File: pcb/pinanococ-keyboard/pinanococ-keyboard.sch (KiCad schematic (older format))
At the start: 70 parts, among them J1 AudioJack4, SW1 SW_Push, SW10 SW_Push, SW11 SW_Push, SW12 SW_Push, SW14 SW_Push, SW15 SW_Push, SW16 SW_Push, SW17 SW_Push, SW18 SW_Push, SW2 SW_Push, SW20 SW_Push_Dual_x2, SW21 SW_Push, SW22 SW_Push, SW23 SW_Push, SW24 SW_Push, SW26 SW_Push_Dual_x2, SW27 SW_Push, SW28 SW_Push, SW29 SW_Push, SW3 SW_Push, SW30 SW_Push, SW32 SW_Push_Dual_x2, SW33 SW_Push, SW34 SW_Push, SW35 SW_Push, SW36 SW_Push, SW37 SW_Push, SW38 Rotary_Encoder_Switch, SW4 SW_Push, SW5 SW_Push, SW6 SW_Push, SW8 SW_Push, SW9 SW_Push, U1 Pico

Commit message: pcb component layout
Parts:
- removed SW14: SW_Push, keyswitches:SW_PG1350, symbol Switch:SW_Push
- added D13: D_ALT, Diode_THT:D_DO-34_SOD68_P7.62mm_Horizontal, symbol Device:D_ALT
- added SW14: SW_Push_Dual_x2, keyswitches:SW_PG1350_double_rotate, symbol Switch:SW_Push_Dual_x2
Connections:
- net COL_2: now also D13.1 (K)
- net ROW_0: now also SW14.4 (D)
- net ROW_1: now also SW14.2 (D)
- net at D14.2 (A): now also SW14.1 (C)
- new net: D13.2 (A), SW14.3 (C)
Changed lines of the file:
@@
-	0    1    1    0
-$EndComp
-$Comp
-L Switch:SW_Push SW14
-U 1 1 61CB00FC
-P 2800 3150
-F 0 "SW14" V 2754 3298 50  0000 L CNN
-F 1 "SW_Push" V 2845 3298 50  0000 L CNN
-F 2 "keyswitches:SW_PG1350" H 2800 3350 50  0001 C CNN
-F 3 "~" H 2800 3350 50  0001 C CNN
-	1    2800 3150
 	0    1    1    0
 $EndComp
@@
 $EndComp
 Connection ~ 2100 3350
-Connection ~ 2800 3350
-Wire Wire Line
-	2100 3350 2800 3350
 Wire Wire Line
 	1400 3350 2100 3350
@@
 	1800 2000 1800 2950
 Wire Wire Line
-	2500 2000 2500 2950
+	2500 2000 2500 2300
 $Comp
 L Device:Rotary_Encoder_Switch SW38
@@
 	4900 3350 5400 3350
 Wire Wire Line
-	1400 2700 3500 2700
-Wire Wire Line
-	2800 3350 3500 3350
+	1400 2700 2800 2700
 $Comp
 L Switch:SW_Push_Dual_x2 SW26
@@
 Wire Wire Line
 	3500 2700 4200 2700
+Wire Wire Line
+	2100 3350 2800 3350
+$Comp
+L Device:D_ALT D13
+U 1 1 61C34EA8
+P 2650 2300
+F 0 "D13" H 2650 2517 50  0000 C CNN
+F 1 "D_ALT" H 2650 2426 50  0000 C CNN
+F 2 "Diode_THT:D_DO-34_SOD68_P7.62mm_Horizontal" H 2650 2300 50  0001 C CNN
+F 3 "~" H 2650 2300 50  0001 C CNN
+	1    2650 2300
+	1    0    0    -1
+$EndComp
+Connection ~ 2500 2300
+Wire Wire Line
+	2500 2300 2500 2950
+$Comp
+L Switch:SW_Push_Dual_x2 SW14
+U 2 1 61C35305
+P 2800 2500
+F 0 "SW14" V 2754 2648 50  0000 L CNN
+F 1 "SW_Push_Dual_x2" V 2845 2648 50  0000 L CNN
+F 2 "keyswitches:SW_PG1350_double_rotate" H 2800 2700 50  0001 C CNN
+F 3 "~" H 2800 2700 50  0001 C CNN
+	2    2800 2500
+	0    1    1    0
+$EndComp
+Connection ~ 2800 2700
+Wire Wire Line
+	2800 2700 3500 2700
+$Comp
+L Switch:SW_Push_Dual_x2 SW14
+U 1 1 61C35B95
+P 2800 3150
+F 0 "SW14" V 2754 3298 50  0000 L CNN
+F 1 "SW_Push_Dual_x2" V 2845 3298 50  0000 L CNN
+F 2 "keyswitches:SW_PG1350_double_rotate" H 2800 3350 50  0001 C CNN
+F 3 "~" H 2800 3350 50  0001 C CNN
+	1    2800 3150
+	0    1    1    0
+$EndComp
+Connection ~ 2800 3350
+Wire Wire Line
+	2800 3350 3500 3350
 $EndSCHEMATC

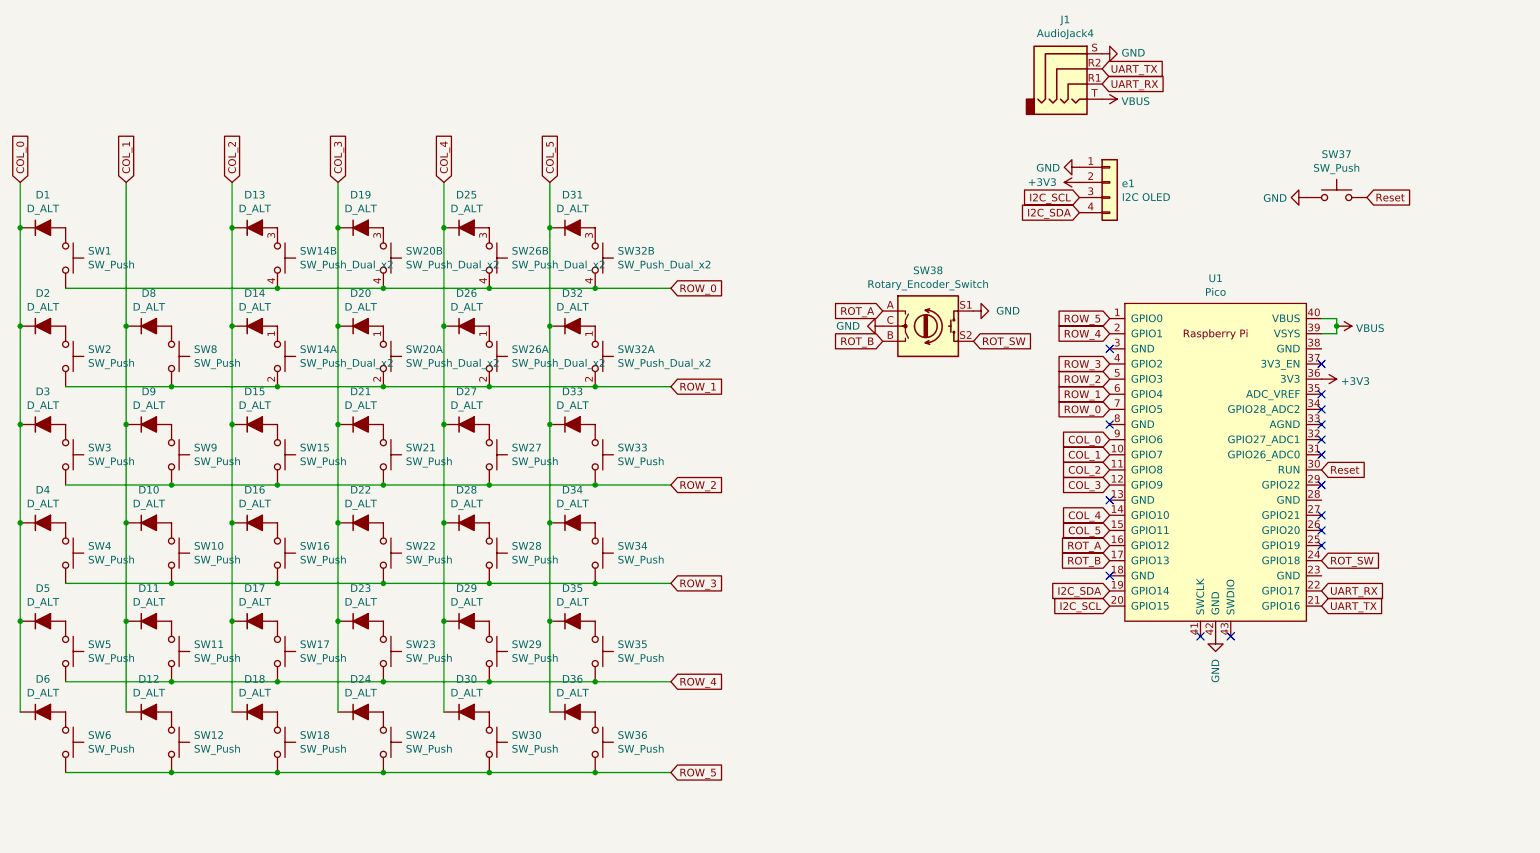
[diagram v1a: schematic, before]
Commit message: inital pcb layout with tracks
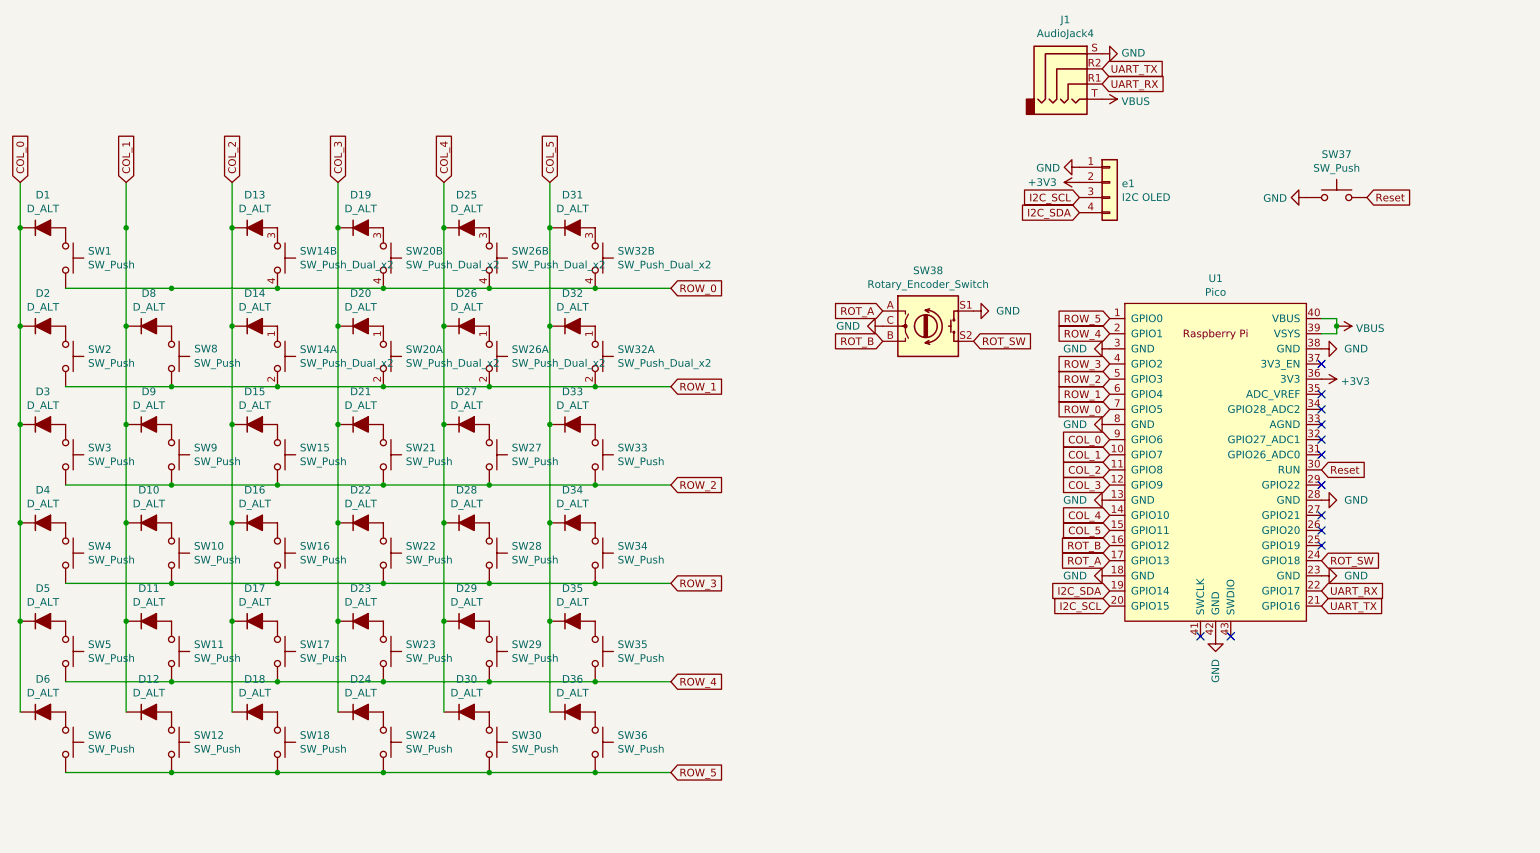
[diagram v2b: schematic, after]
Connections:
- net GND: now also U1.13 (GND), U1.18 (GND), U1.23 (GND), U1.28 (GND), U1.3 (GND), U1.38 (GND), U1.8 (GND)
- net ROT_A: now also U1.17 (GPIO13); no longer U1.16 (GPIO12)
- net ROT_B: now also U1.16 (GPIO12); no longer U1.17 (GPIO13)
- no-connect marks 16 -> 12
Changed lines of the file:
@@
 NoConn ~ 9700 3200
 NoConn ~ 9700 3400
-NoConn ~ 8300 3100
-NoConn ~ 8300 4600
-NoConn ~ 8300 4100
-NoConn ~ 8300 3600
 NoConn ~ 9700 3600
 Text GLabel 9700 4800 2    50   Input ~ 0
@@
 U 1 1 61CB00F6
 P 2100 3150
-F 0 "SW8" V 2054 3298 50  0000 L CNN
+F 0 "SW8" V 2050 3300 50  0000 L CNN
 F 1 "SW_Push" V 2145 3298 50  0000 L CNN
 F 2 "keyswitches:SW_PG1350" H 2100 3350 50  0001 C CNN
@@
 NoConn ~ 9700 3500
 Wire Wire Line
-	1800 2000 1800 2950
+	1800 2000 1800 2300
 Wire Wire Line
 	2500 2000 2500 2300
@@
 	0    1    1    0
 $EndComp
+Text GLabel 8300 4500 0    50   Input ~ 0
+ROT_A
 Text GLabel 8300 4400 0    50   Input ~ 0
-ROT_A
-Text GLabel 8300 4500 0    50   Input ~ 0
 ROT_B
 $Comp
@@
 Wire Wire Line
 	4900 3350 5400 3350
-Wire Wire Line
-	1400 2700 2800 2700
 $Comp
 L Switch:SW_Push_Dual_x2 SW26
@@
 Wire Wire Line
 	2800 3350 3500 3350
+Connection ~ 1800 2300
+Wire Wire Line
+	1800 2300 1800 2950
+Connection ~ 2100 2700
+Wire Wire Line
+	2100 2700 2800 2700
+Wire Wire Line
+	1400 2700 2100 2700
+$Comp
+L power:GND #PWR?
+U 1 1 61CBF1FB
+P 8300 3100
+F 0 "#PWR?" H 8300 2850 50  0001 C CNN
+F 1 "GND" V 8300 2950 50  0000 R CNN
+F 2 "" H 8300 3100 50  0001 C CNN
+F 3 "" H 8300 3100 50  0001 C CNN
+	1    8300 3100
+	0    1    1    0
+$EndComp
+$Comp
+L power:GND #PWR?
+U 1 1 61CC13E9
+P 8300 3600
+F 0 "#PWR?" H 8300 3350 50  0001 C CNN
+F 1 "GND" V 8300 3450 50  0000 R CNN
+F 2 "" H 8300 3600 50  0001 C CNN
+F 3 "" H 8300 3600 50  0001 C CNN
+	1    8300 3600
+	0    1    1    0
+$EndComp
+$Comp
+L power:GND #PWR?
+U 1 1 61CC1677
+P 8300 4100
+F 0 "#PWR?" H 8300 3850 50  0001 C CNN
+F 1 "GND" V 8300 3950 50  0000 R CNN
+F 2 "" H 8300 4100 50  0001 C CNN
+F 3 "" H 8300 4100 50  0001 C CNN
+	1    8300 4100
+	0    1    1    0
+$EndComp
+$Comp
+L power:GND #PWR?
+U 1 1 61CC1AD9
+P 8300 4600
+F 0 "#PWR?" H 8300 4350 50  0001 C CNN
+F 1 "GND" V 8300 4450 50  0000 R CNN
+F 2 "" H 8300 4600 50  0001 C CNN
+F 3 "" H 8300 4600 50  0001 C CNN
+	1    8300 4600
+	0    1    1    0
+$EndComp
+$Comp
+L power:GND #PWR?
+U 1 1 61CC1DF0
+P 9700 4600
+F 0 "#PWR?" H 9700 4350 50  0001 C CNN
+F 1 "GND" V 9700 4450 50  0000 R CNN
+F 2 "" H 9700 4600 50  0001 C CNN
+F 3 "" H 9700 4600 50  0001 C CNN
+	1    9700 4600
+	0    -1   -1   0
+$EndComp
+$Comp
+L power:GND #PWR?
+U 1 1 61CC27D8
+P 9700 4100
+F 0 "#PWR?" H 9700 3850 50  0001 C CNN
+F 1 "GND" V 9700 3950 50  0000 R CNN
+F 2 "" H 9700 4100 50  0001 C CNN
+F 3 "" H 9700 4100 50  0001 C CNN
+	1    9700 4100
+	0    -1   -1   0
+$EndComp
+$Comp
+L power:GND #PWR?
+U 1 1 61CC2DE6
+P 9700 3100
+F 0 "#PWR?" H 9700 2850 50  0001 C CNN
+F 1 "GND" V 9700 2950 50  0000 R CNN
+F 2 "" H 9700 3100 50  0001 C CNN
+F 3 "" H 9700 3100 50  0001 C CNN
+	1    9700 3100
+	0    -1   -1   0
+$EndComp
 $EndSCHEMATC

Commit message: reannotated flippable schematic
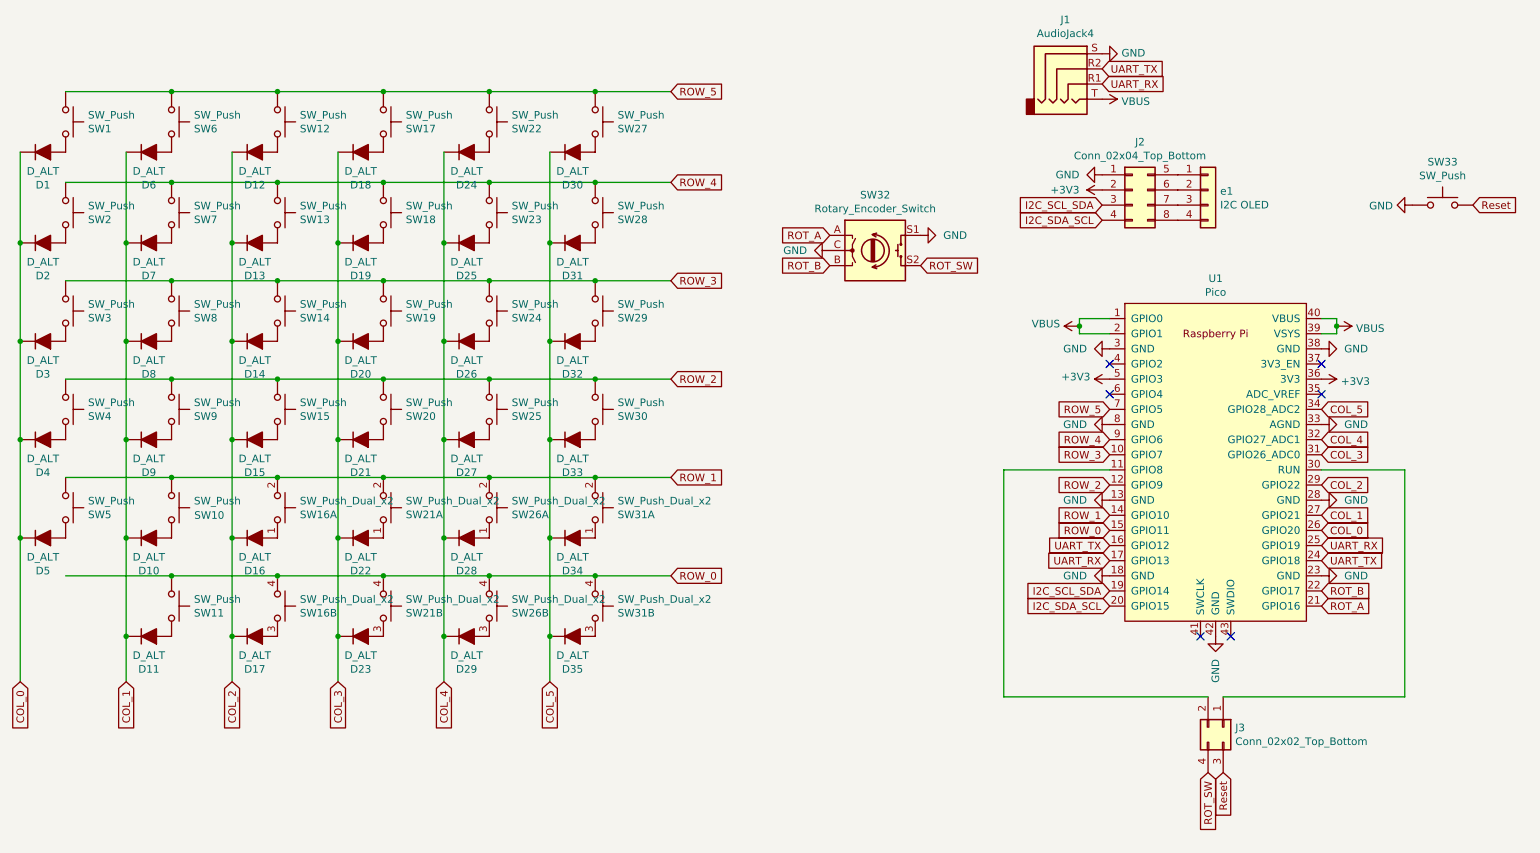
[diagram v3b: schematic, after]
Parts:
- added J2: Conn_02x04_Top_Bottom, symbol Connector_Generic:Conn_02x04_Top_Bottom
- added J3: Conn_02x02_Top_Bottom, symbol Connector_Generic:Conn_02x02_Top_Bottom
- renumbered D6 to D1, D8 to D10, D1 to D11, D18 to D12, D17 to D13, D16 to D14, D14 to D16, D13 to D17, D24 to D18, D23 to D19, D5 to D2, D22 to D20, D20 to D22, D19 to D23, D30 to D24, D29 to D25, D28 to D26, D26 to D28, D25 to D29, D4 to D3, D36 to D30, D35 to D31, D34 to D32, D32 to D34, D31 to D35, D3 to D4, D2 to D5, D12 to D6, D11 to D7, D10 to D8, SW6 to SW1, SW8 to SW10, SW1 to SW11, SW18 to SW12, SW17 to SW13, SW16 to SW14, SW14 to SW16, SW24 to SW17, SW23 to SW18, SW22 to SW19, SW5 to SW2, SW21 to SW20, SW20 to SW21, SW30 to SW22, SW29 to SW23, SW28 to SW24, SW27 to SW25, SW36 to SW27, SW35 to SW28, SW34 to SW29, SW4 to SW3, SW33 to SW30, SW32 to SW31, SW38 to SW32, SW37 to SW33, SW3 to SW4, SW2 to SW5, SW12 to SW6, SW11 to SW7, SW10 to SW8
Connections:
- net +3V3: now also U1.5 (GPIO3), J2.2 (Pin_2); no longer e1.2 (Pin_2)
- net COL_0: now also U1.26 (GPIO20); no longer D11.1 (K), U1.9 (GPIO6)
- net COL_1: now also D11.1 (K), U1.27 (GPIO21); no longer U1.10 (GPIO7)
- net COL_2: now also U1.29 (GPIO22); no longer U1.11 (GPIO8)
- net COL_3: now also U1.31 (GPIO26_ADC0); no longer U1.12 (GPIO9)
- net COL_4: now also U1.32 (GPIO27_ADC1); no longer U1.14 (GPIO10)
- net COL_5: now also U1.34 (GPIO28_ADC2); no longer U1.15 (GPIO11)
- net GND: now also U1.33 (AGND), J2.1 (Pin_1); no longer e1.1 (Pin_1)
- net ROT_A: now also U1.21 (GPIO16); no longer U1.17 (GPIO13)
- net ROT_B: now also U1.22 (GPIO17); no longer U1.16 (GPIO12)
- net ROT_SW: now also J3.4 (Pin_4); no longer U1.24 (GPIO18)
- net ROW_0: now also U1.15 (GPIO11); no longer U1.7 (GPIO5)
- net ROW_1: now also U1.14 (GPIO10); no longer U1.6 (GPIO4)
- net ROW_2: now also U1.12 (GPIO9); no longer U1.5 (GPIO3)
- net ROW_3: now also U1.10 (GPIO7); no longer U1.4 (GPIO2)
- net ROW_4: now also U1.9 (GPIO6); no longer U1.2 (GPIO1)
- net ROW_5: now also U1.7 (GPIO5); no longer U1.1 (GPIO0)
- net Reset: now also J3.3 (Pin_3); no longer U1.30 (RUN)
- net UART_RX: now also U1.17 (GPIO13), U1.25 (GPIO19); no longer U1.22 (GPIO17)
- net UART_TX: now also U1.16 (GPIO12), U1.24 (GPIO18); no longer U1.21 (GPIO16)
- net VBUS: now also U1.1 (GPIO0), U1.2 (GPIO1)
- net I2C_SCL: no longer names the net of e1.3 (Pin_3)
- net I2C_SCL: now also J2.7 (Pin_7); no longer U1.20 (GPIO15)
- net I2C_SDA: no longer names the net of e1.4 (Pin_4)
- net I2C_SDA: now also J2.8 (Pin_8); no longer U1.19 (GPIO14)
- new net: J3.1 (Pin_1), U1.30 (RUN)
- new net: J3.2 (Pin_2), U1.11 (GPIO8)
- new net: J2.5 (Pin_5), e1.1 (Pin_1)
- new net: J2.6 (Pin_6), e1.2 (Pin_2)
- new net I2C_SCL_SDA: J2.3 (Pin_3), U1.19 (GPIO14)
- new net I2C_SDA_SCL: J2.4 (Pin_4), U1.20 (GPIO15)
- no-connect marks 12 -> 6
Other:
- moved on the sheet: D1, D10, D11, D12, D13, D14, D15, D16, D17, D18, D19, D2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

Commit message: first draft flipable footprints with scematic
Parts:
- D1, D10, D11, D12, D13, D14, D15, D16, D17, D18, D19, D2, D20, D21, D22, D23, D24, D25, D26, D27, D28, D29, D3, D30, D31, D32, D33, D34, D35, D4, D5, D6, D7, D8, D9: footprint Diode_THT:D_DO-34_SOD68_P7.62mm_Horizontal -> Diode_THT:D_DO-35_SOD27_P7.62mm_Horizontal
- J1: footprint Connector_Audio:Jack_3.5mm_PJ320E_Horizontal -> footprints:TRRS-PJ-320A_reversable
- J2: footprint (none) -> Connector_PinHeader_2.54mm:PinHeader_2x04_P2.54mm_Vertical
- J3: footprint (none) -> Connector_PinHeader_2.54mm:PinHeader_2x02_P2.54mm_Vertical
- SW1, SW10, SW11, SW12, SW13, SW14, SW15, SW17, SW18, SW19, SW2, SW20, SW22, SW23, SW24, SW25, SW27, SW28, SW29, SW3, SW30, SW4, SW5, SW6, SW7, SW8, SW9: footprint keyswitches:SW_PG1350 -> keyswitches:SW_PG1350_reversible
- SW16, SW21, SW26, SW31: footprint keyswitches:SW_PG1350_double_rotate -> footprints:SW_PG1350_reversible_double_rotatable
- SW32: footprint Rotary_Encoder:RotaryEncoder_Alps_EC12E-Switch_Vertical_H20mm -> Rotary_Encoder:RotaryEncoder_Alps_EC11E-Switch_Vertical_H20mm
- U1: footprint MCU_RaspberryPi_and_Boards:RPi_Pico_SMD_TH -> footprints:RPi_Pico_SMD_TH_flipable
- e1: footprint Connector_PinSocket_2.54mm:PinSocket_1x04_P2.54mm_Vertical -> Connector_PinHeader_2.54mm:PinHeader_1x04_P2.54mm_Vertical

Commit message: inital switch pcb layout
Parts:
- J2: symbol Connector_Generic:Conn_02x04_Top_Bottom -> Connector_Generic:Conn_02x04_Odd_Even
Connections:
- net +3V3: now also J2.3 (Pin_3); no longer J2.2 (Pin_2)
- net I2C_SCL_SDA: now also J2.5 (Pin_5); no longer J2.3 (Pin_3)
- net I2C_SDA_SCL: now also J2.7 (Pin_7); no longer J2.4 (Pin_4)
- net at e1.1 (Pin_1): now also J2.2 (Pin_2); no longer J2.5 (Pin_5)
- net at e1.2 (Pin_2): now also J2.4 (Pin_4); no longer J2.6 (Pin_6)
- net at e1.3 (Pin_3): now also J2.6 (Pin_6); no longer J2.7 (Pin_7)
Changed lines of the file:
@@
 	7600 3900 8300 3900
 $Comp
-L Connector_Generic:Conn_02x04_Top_Bottom J2
+L Connector_Generic:Conn_02x04_Odd_Even J2
 U 1 1 61C5EAE6
 P 8450 2050
